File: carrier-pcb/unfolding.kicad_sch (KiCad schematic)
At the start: 59 parts, among them J1 USB_C_Receptacle_USB2.0, J2 USB_B_Micro, J3 Conn_02x09_Odd_Even, U1 TCA9548APWR, U10 DRV2605LDGS, U11 DRV2605LDGS, U2 TCA9548APWR, U3 DRV2605LDGS, U4 DRV2605LDGS, U5 DRV2605LDGS, U6 DRV2605LDGS, U7 DRV2605LDGS, U8 DRV2605LDGS, U9 DRV2605LDGS

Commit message: Add 3rd_party_libs folder and place footrpints and symbols. Place bmx160 and TE IDC connector. Add route_try file to try out routing.
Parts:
- removed J2: USB_B_Micro, Connector_USB:USB_Micro-B_Amphenol_10104110_Horizontal, symbol Connector:USB_B_Micro
- removed J3: Conn_02x09_Odd_Even, Connector_PinHeader_2.54mm:PinHeader_2x09_P2.54mm_Horizontal, symbol Connector_Generic:Conn_02x09_Odd_Even
- added C21: 100n, Capacitor_SMD:C_0603_1608Metric, symbol Device:C_Small
- added D1: RND SMBJ5A, Diode_SMD:D_0603_1608Metric, symbol pspice:DIODE
- added J2: Conn_01x04_Female, Connector_Wire:SolderWire-0.1sqmm_1x04_P3.6mm_D0.4mm_OD1mm, symbol Connector:Conn_01x04_Female
- added J3: 1-338068-8, footprints:1-338068-8, symbol 2021-04-16_16-40-50:1-338068-8
- added JP1: SolderJumper_2_Open, Jumper:SolderJumper-2_P1.3mm_Open_RoundedPad1.0x1.5mm, symbol Jumper:SolderJumper_2_Open
- added R25, R26, R27: 2K2, Resistor_SMD:R_0603_1608Metric, symbol Device:R_Small
- added U12: BMX160, BMX160:PQFN50P250X300X100-14N, symbol BMX160:BMX160
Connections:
- net +3V3: now also C21.1, R25.1, R26.1, U12.12 (CSB), U12.5 (VDDIO), U12.8 (VDD)
- net +5V: now also D1.2 (A), J2.4 (Pin_4)
- net GND: now also C21.2, D1.1 (K), J2.1 (Pin_1), JP1.2 (B), R27.2, U12.2 (GND), U12.3 (GND), U12.6 (GNDIO), U12.7 (GND)
- net M1+: now also J3.1
- net M1-: now also J3.2
- net M2+: now also J3.3
- net M2-: now also J3.4
- net M3+: now also J3.5
- net M3-: now also J3.6
- net M4+: now also J3.7
- net M4-: now also J3.8
- net M5+: now also J3.9
- net M5-: now also J3.10
- net M6+: now also J3.11
- net M6-: now also J3.12
- net M7+: now also J3.13
- net M7-: now also J3.14
- net M8+: now also J3.15
- net M8-: now also J3.16
- net M9+: now also J3.17
- net M9-: now also J3.18
- net USB_D+: now also J2.3 (Pin_3)
- net USB_D-: now also J2.2 (Pin_2)
- net SDA_bmx160: now reaches U2.19 (SD7)
- net SDA_bmx160: now also R25.2, U12.14 (SDX)
- net SCL_bmx160: now reaches U2.20 (SC7)
- net SCL_bmx160: now also R26.2, U12.13 (SCX)
- net EEPROM_nWP: now reaches Module1.20 (EEPROM_nWP)
- net EEPROM_nWP: now also JP1.1 (A)
- net Global_EN: no longer names the net of Module1.99 (Global_EN)
- net USB_ID: no longer names the net of Module1.101 (USB_OTG_ID)
- net ~EXTRST: no longer names the net of Module1.100 (nEXTRST)
- net ~RPIBOOT: no longer names the net of Module1.93 (nRPIBOOT)
- new net: R27.1, U12.1 (SDO)
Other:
- note added: "18 pin IDC plug from TE"
- note added: "2x i2c multiplexer"
- note added: "9 axis: gyro, acc, magn"
- note added: "9x motor driver 2605l"
- note added: "Close for EEPROM write protection"
- note added: "pads to connect micro USB 3.0 male plug glued to the board"

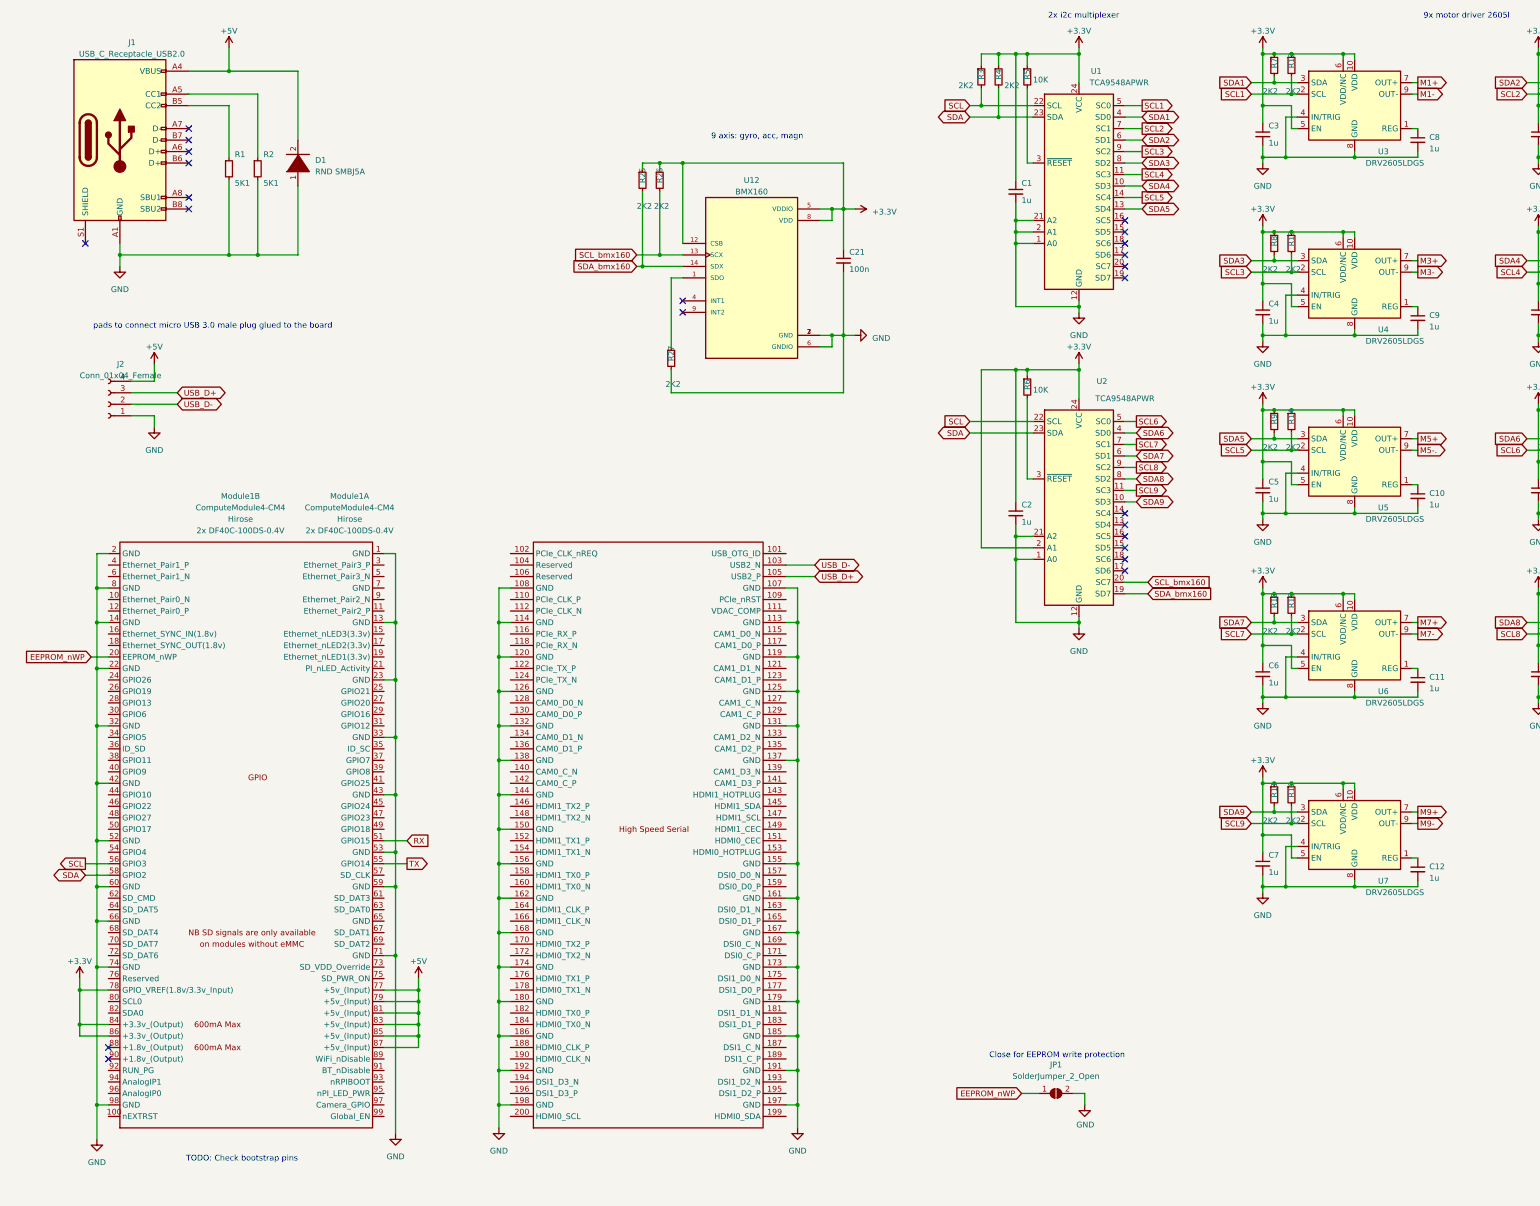
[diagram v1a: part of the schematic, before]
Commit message: removed more backups and renamed files. USE MORE BRANCHES, DONT RENAME
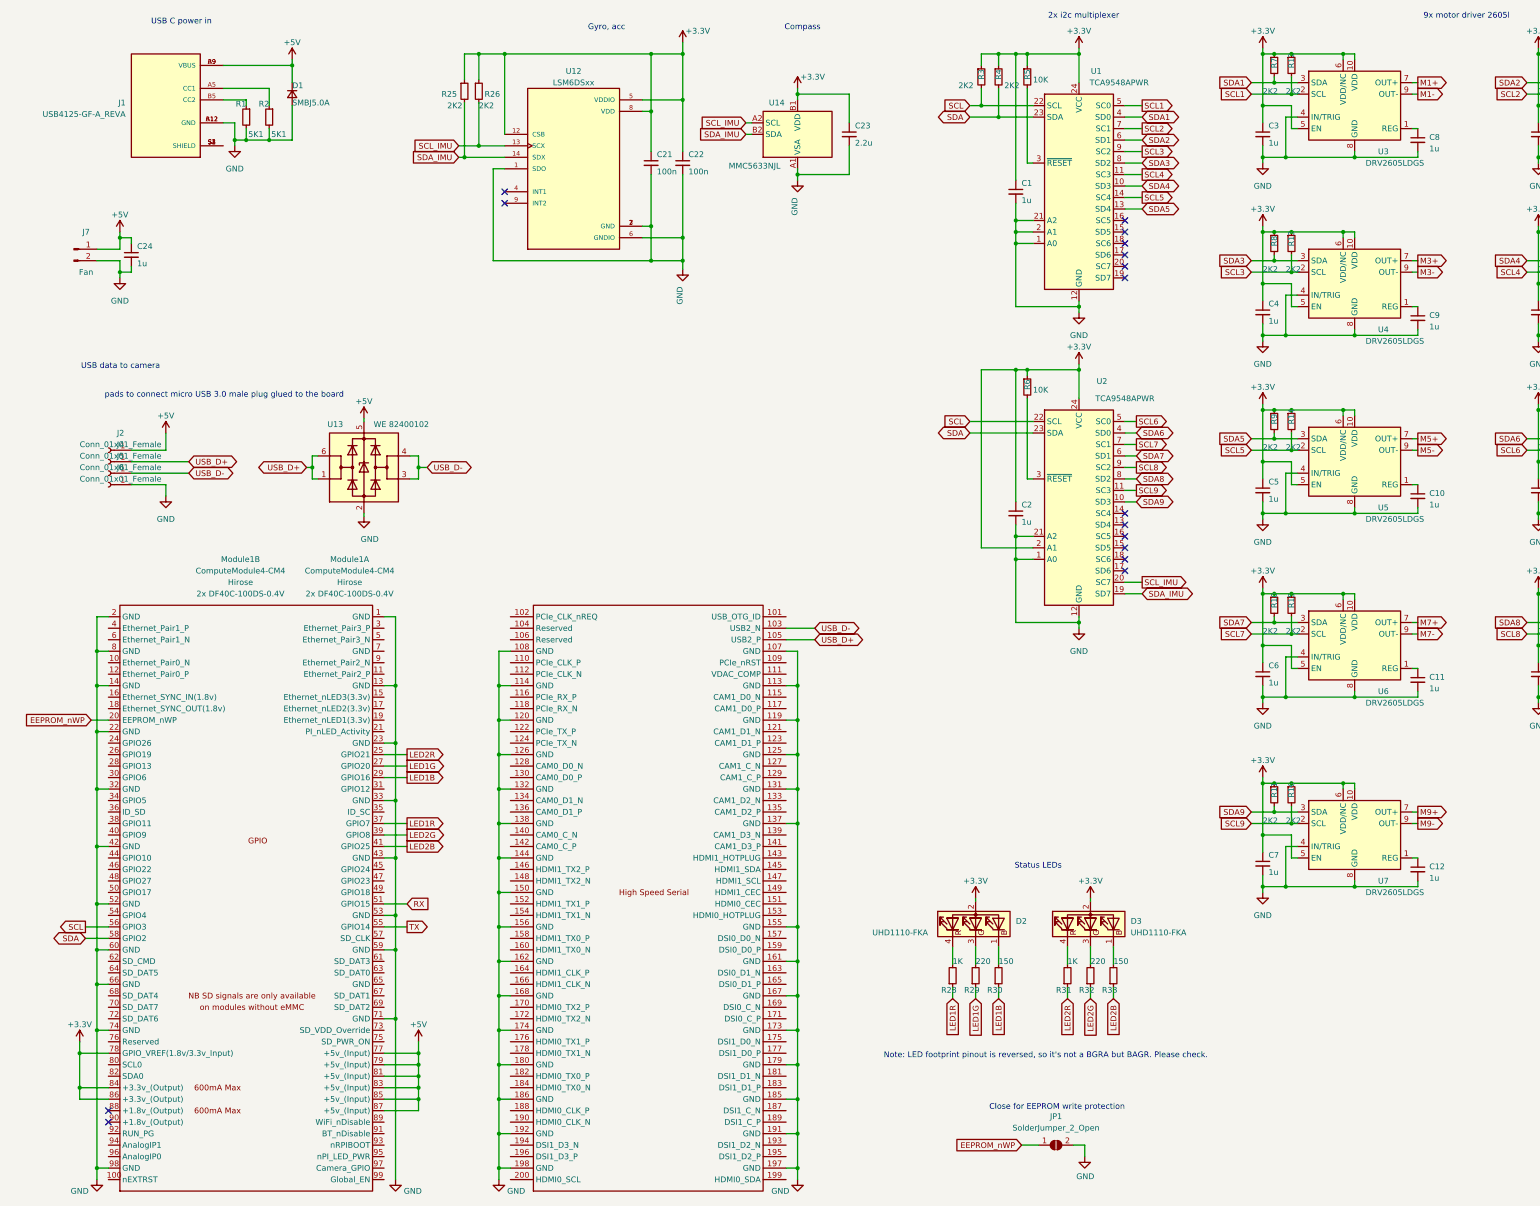
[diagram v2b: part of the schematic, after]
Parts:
- removed D1: RND SMBJ5A, Diode_SMD:D_0603_1608Metric, symbol pspice:DIODE
- removed J1: USB_C_Receptacle_USB2.0, Connector_USB:USB_C_Receptacle_HRO_TYPE-C-31-M-12, symbol Connector:USB_C_Receptacle_USB2.0
- removed J2: Conn_01x04_Female, Connector_Wire:SolderWire-0.1sqmm_1x04_P3.6mm_D0.4mm_OD1mm, symbol Connector:Conn_01x04_Female
- removed R27: 2K2, Resistor_SMD:R_0603_1608Metric, symbol Device:R_Small
- added C22: 100n, Capacitor_SMD:C_0603_1608Metric, symbol Device:C_Small
- added C23: 2.2u, Capacitor_SMD:C_0603_1608Metric, symbol Device:C_Small
- added C24: 1u, Capacitor_SMD:C_0603_1608Metric, symbol Device:C_Small
- added D1: SMBJ5.0A, Diode_SMD:D_SMA, symbol Device:D_Small
- added D2, D3: UHD1110-FKA, LED_SMD:LED_Lumex_SML-LX0404SIUPGUSB, symbol Device:LED_BAGR
- added J1: USB4125-GF-A_REVA, USB4125-GF-A_REVA:GCT_USB4125-GF-A_REVA, symbol USB4125-GF-A_REVA:USB4125-GF-A_REVA
- added J2, J4, J5, J6: Conn_01x01_Female, Connector_Wire:SolderWirePad_1x01_SMD_1x2mm, symbol Connector:Conn_01x01_Female
- added J7: Fan, Pico-Spox:PICOspox-2-v, symbol Connector:Conn_01x02_Male
- added R28, R31: 1K, Resistor_SMD:R_0603_1608Metric, symbol Device:R_Small
- added R29, R32: 220, Resistor_SMD:R_0603_1608Metric, symbol Device:R_Small
- added R30, R33: 150, Resistor_SMD:R_0603_1608Metric, symbol Device:R_Small
- added U13: WE 82400102, Package_TO_SOT_SMD:SOT-23-6, symbol Power_Protection:USBLC6-2SC6
- added U14: MMC5633NJL, Package_BGA:WLP-4_0.86x0.86mm_P0.4mm, symbol Sensor_Magnetic:MMC5633NJL
- U1, U10, U11, U2, U3, U4, U5, U6, U7, U8, U9: MF (none) -> TI
- U12: value BMX160 -> LSM6DSxx; MF Bosch -> ST Micro
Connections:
- net M5-. is gone; now on net M5-: U5.9 (OUT-)
- net +3V3: now also C22.1, C23.1, D2.2 (A), D3.2 (A), U14.B1 (VDD)
- net +5V: now also C24.1, D1.1 (K), J1.A9 (VBUS), J1.B9 (VBUS), J2.1 (Pin_1), J7.1 (Pin_1), U13.5 (VBUS)
- net GND: now also U12.1 (SDO), C22.2, C23.2, C24.2, D1.2 (A), J1.A12 (GND), J1.B12 (GND), J6.1 (Pin_1), J7.2 (Pin_2), U13.2 (GND), U14.A1 (VSA)
- net USB_D+: now also J4.1 (Pin_1), U13.1 (I/O1), U13.6 (I/O1)
- net USB_D-: now also J5.1 (Pin_1), U13.3 (I/O2), U13.4 (I/O2)
- net at R2.1: now also J1.A5 (CC1)
- net at R1.1: now also J1.B5 (CC2)
- net LED2R: now reaches Module1.25 (GPIO21)
- net LED2R: now also R31.1
- net LED1G: now reaches Module1.27 (GPIO20)
- net LED1G: now also R29.1
- net LED1B: now reaches Module1.29 (GPIO16)
- net LED1B: now also R30.1
- net LED1R: now reaches Module1.37 (GPIO7)
- net LED1R: now also R28.1
- net LED2G: now reaches Module1.39 (GPIO8)
- net LED2G: now also R32.1
- net LED2B: now reaches Module1.41 (GPIO25)
- net LED2B: now also R33.1
- net SCL_bmx160 renamed SCL_IMU
- net SCL_IMU: now also U14.A2 (SCL)
- net SDA_bmx160 renamed SDA_IMU
- net SDA_IMU: now also U14.B2 (SDA)
- new net: J1.S1 (SHIELD), J1.S2 (SHIELD), J1.S3 (SHIELD), J1.S4 (SHIELD)
- new net: D2.1 (BK), R30.2
- new net: D2.4 (RK), R28.2
- new net: D3.1 (BK), R33.2
- new net: D3.3 (GK), R32.2
- new net: D3.4 (RK), R31.2
- new net: D2.3 (GK), R29.2
- no-connect marks 23 -> 16
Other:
- note added: "Compass"
- note added: "Gyro, acc"
- note added: "Note: LED footprint pinout is reversed, so it's not a BGRA but BAGR. Please check."
- note added: "Status LEDs"
- note added: "USB C power in"
- note added: "USB data to camera"
- note removed: "9 axis: gyro, acc, magn"
- note removed: "TODO: Check bootstrap pins"
- moved on the sheet: C21, JP1, Module1A, Module1B, R1, R2, R25, R26, U12
